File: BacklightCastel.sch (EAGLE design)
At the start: 7 parts, among them U1 TLV61046A

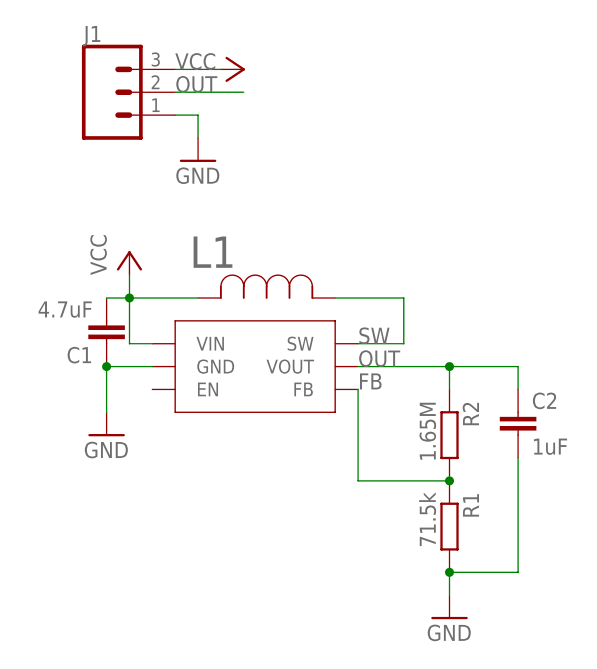
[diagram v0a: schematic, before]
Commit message: Layout update
Moved output capacitor, swapped R1 & R2, tied EN to VCC
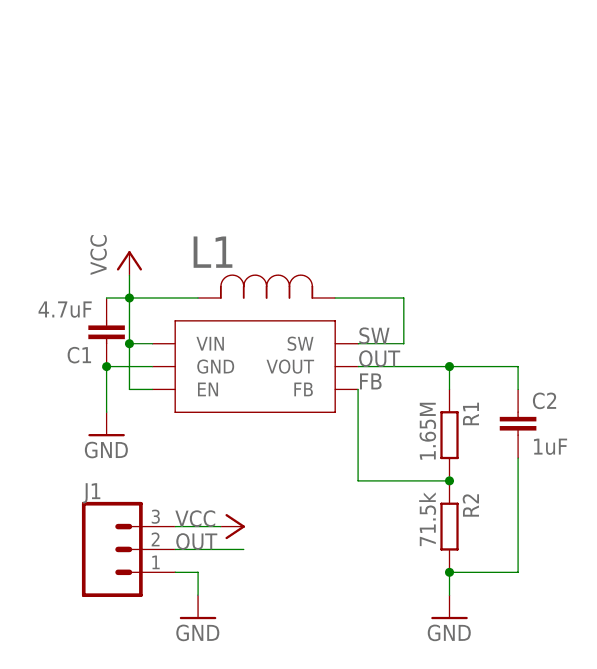
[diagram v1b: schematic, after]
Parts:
- L1: value NRS5020T220MMGJ -> 22uH
- R1: value 71.5k -> 1.65M
- R2: value 1.65M -> 71.5k
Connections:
- net FB: now also R1.2, R2.1; no longer R1.1, R2.2
- net GND: now also R2.2; no longer R1.2
- net OUT: now also R1.1; no longer R2.1
- net VCC: now also U1.EN
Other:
- moved on the sheet: J1, R1, R2
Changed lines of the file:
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@@
 <part name="P+7" library="supply1" library_urn="urn:adsk.eagle:library:371" deviceset="VCC" device=""/>
 <part name="GND8" library="supply1" library_urn="urn:adsk.eagle:library:371" deviceset="GND" device=""/>
-<part name="L1" library="dsl" deviceset="NRS5020T220MMGJ" device=""/>
-<part name="R2" library="resistor" library_urn="urn:adsk.eagle:library:348" deviceset="R-EU_" device="R0603" package3d_urn="urn:adsk.eagle:package:23555/2" value="1.65M"/>
-<part name="R1" library="resistor" library_urn="urn:adsk.eagle:library:348" deviceset="R-EU_" device="R0603" package3d_urn="urn:adsk.eagle:package:23555/2" value="71.5k"/>
+<part name="L1" library="dsl" deviceset="NRS5020T220MMGJ" device="" value="22uH"/>
+<part name="R1" library="resistor" library_urn="urn:adsk.eagle:library:348" deviceset="R-EU_" device="R0603" package3d_urn="urn:adsk.eagle:package:23555/2" value="1.65M"/>
+<part name="R2" library="resistor" library_urn="urn:adsk.eagle:library:348" deviceset="R-EU_" device="R0603" package3d_urn="urn:adsk.eagle:package:23555/2" value="71.5k"/>
 <part name="GND9" library="supply1" library_urn="urn:adsk.eagle:library:371" deviceset="GND" device=""/>
 <part name="C2" library="rcl" library_urn="urn:adsk.eagle:library:334" deviceset="C-EU" device="C0603" package3d_urn="urn:adsk.eagle:package:23616/2" value="1uF"/>
@@
 <attribute name="NAME" x="16.8656" y="41.4528" size="3.4798" layer="95" ratio="10" rot="SR0"/>
 </instance>
-<instance part="R2" gate="G$1" x="45.72" y="22.86" smashed="yes" rot="R270">
+<instance part="R1" gate="G$1" x="45.72" y="22.86" smashed="yes" rot="R270">
 <attribute name="NAME" x="47.2186" y="26.67" size="1.778" layer="95" rot="R270"/>
 <attribute name="VALUE" x="42.418" y="26.67" size="1.778" layer="96" rot="R270"/>
 </instance>
-<instance part="R1" gate="G$1" x="45.72" y="12.7" smashed="yes" rot="R270">
+<instance part="R2" gate="G$1" x="45.72" y="12.7" smashed="yes" rot="R270">
 <attribute name="NAME" x="47.2186" y="16.51" size="1.778" layer="95" rot="R270"/>
 <attribute name="VALUE" x="42.418" y="16.51" size="1.778" layer="96" rot="R270"/>
@@
 <attribute name="VALUE" x="6.096" y="37.719" size="1.778" layer="96" rot="R180"/>
 </instance>
-<instance part="J1" gate="J$1" x="7.62" y="60.96" smashed="yes">
-<attribute name="VALUE" x="5.08" y="53.594" size="1.778" layer="96" font="vector"/>
-<attribute name="NAME" x="5.08" y="66.548" size="1.778" layer="95" font="vector"/>
+<instance part="J1" gate="J$1" x="7.62" y="10.16" smashed="yes">
+<attribute name="VALUE" x="5.08" y="2.794" size="1.778" layer="96" font="vector"/>
+<attribute name="NAME" x="5.08" y="15.748" size="1.778" layer="95" font="vector"/>
 </instance>
-<instance part="GND1" gate="1" x="17.78" y="53.34" smashed="yes">
-<attribute name="VALUE" x="15.24" y="50.8" size="1.778" layer="96"/>
+<instance part="GND1" gate="1" x="17.78" y="2.54" smashed="yes">
+<attribute name="VALUE" x="15.24" y="0" size="1.778" layer="96"/>
 </instance>
-<instance part="P+1" gate="VCC" x="22.86" y="63.5" smashed="yes" rot="R270">
-<attribute name="VALUE" x="15.24" y="63.5" size="1.778" layer="96"/>
+<instance part="P+1" gate="VCC" x="22.86" y="12.7" smashed="yes" rot="R270">
+<attribute name="VALUE" x="15.24" y="12.7" size="1.778" layer="96"/>
 </instance>
 </instances>
@@
 <segment>
 <pinref part="GND9" gate="1" pin="GND"/>
-<pinref part="R1" gate="G$1" pin="2"/>
+<pinref part="R2" gate="G$1" pin="2"/>
 <wire x1="45.72" y1="5.08" x2="45.72" y2="7.62" width="0.1524" layer="91"/>
 <pinref part="C2" gate="G$1" pin="2"/>
@@
 <pinref part="J1" gate="J$1" pin="1"/>
 <pinref part="GND1" gate="1" pin="GND"/>
-<wire x1="15.24" y1="58.42" x2="17.78" y2="58.42" width="0.1524" layer="91"/>
-<wire x1="17.78" y1="58.42" x2="17.78" y2="55.88" width="0.1524" layer="91"/>
+<wire x1="15.24" y1="7.62" x2="17.78" y2="7.62" width="0.1524" layer="91"/>
+<wire x1="17.78" y1="7.62" x2="17.78" y2="5.08" width="0.1524" layer="91"/>
 </segment>
 </net>
@@
 <pinref part="C1" gate="G$1" pin="2"/>
 <wire x1="7.62" y1="38.1" x2="10.16" y2="38.1" width="0.1524" layer="91"/>
+<pinref part="U1" gate="G$1" pin="EN"/>
+<wire x1="12.7" y1="27.94" x2="10.16" y2="27.94" width="0.1524" layer="91"/>
+<wire x1="10.16" y1="27.94" x2="10.16" y2="33.02" width="0.1524" layer="91"/>
+<junction x="10.16" y="33.02"/>
 </segment>
 <segment>
 <pinref part="J1" gate="J$1" pin="3"/>
 <pinref part="P+1" gate="VCC" pin="VCC"/>
-<wire x1="15.24" y1="63.5" x2="20.32" y2="63.5" width="0.1524" layer="91"/>
+<wire x1="15.24" y1="12.7" x2="20.32" y2="12.7" width="0.1524" layer="91"/>
 </segment>
 </net>
@@
 <net name="FB" class="0">
 <segment>
-<pinref part="R2" gate="G$1" pin="2"/>
-<pinref part="R1" gate="G$1" pin="1"/>
+<pinref part="R1" gate="G$1" pin="2"/>
+<pinref part="R2" gate="G$1" pin="1"/>
 <pinref part="U1" gate="G$1" pin="FB"/>
 <wire x1="45.72" y1="17.78" x2="35.56" y2="17.78" width="0.1524" layer="91"/>
@@
 <net name="OUT" class="0">
 <segment>
-<pinref part="R2" gate="G$1" pin="1"/>
+<pinref part="R1" gate="G$1" pin="1"/>
 <pinref part="U1" gate="G$1" pin="VOUT"/>
 <wire x1="45.72" y1="27.94" x2="45.72" y2="30.48" width="0.1524" layer="91"/>
@@
 <segment>
 <pinref part="J1" gate="J$1" pin="2"/>
-<wire x1="15.24" y1="60.96" x2="22.86" y2="60.96" width="0.1524" layer="91"/>
-<label x="15.24" y="60.96" size="1.778" layer="95"/>
+<wire x1="15.24" y1="10.16" x2="22.86" y2="10.16" width="0.1524" layer="91"/>
+<label x="15.24" y="10.16" size="1.778" layer="95"/>
 </segment>
 </net>
